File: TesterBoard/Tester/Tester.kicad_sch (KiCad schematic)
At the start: 18 parts, among them Q1 LM7805CT_NOPB, SW1 SW_DIP_x04, U1 74HC14N, U2 Z80CPU

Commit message: oscillator
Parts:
- added Y1: ATS08A-E, ATS08A-E:XTAL_HC49P488W43L1085T450H368, symbol ATS08A-E:ATS08A-E
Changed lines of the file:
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@@
+	)
+	(symbol
+		(lib_id "ATS08A-E:ATS08A-E")
+		(at 142.24 87.63 0)
+		(unit 1)
+		(exclude_from_sim no)
+		(in_bom yes)
+		(on_board yes)
+		(dnp no)
+		(fields_autoplaced yes)
+		(property "Reference" "Y1"
+			(at 142.24 80.01 0)
+			(effects
+				(font
+					(size 1.27 1.27)
+				)
+			)
+		)
+		(property "Value" "ATS08A-E"
+			(at 142.24 82.55 0)
+			(effects
+				(font
+					(size 1.27 1.27)
+				)
+			)
+		)
+		(property "Footprint" "ATS08A-E:XTAL_HC49P488W43L1085T450H368"
+			(at 142.24 87.63 0)
+			(effects
+				(font
+					(size 1.27 1.27)
+				)
+				(justify bottom)
+				(hide yes)
+			)
+		)
+		(property "Datasheet" ""
+			(at 142.24 87.63 0)
+			(effects
+				(font
+					(size 1.27 1.27)
+				)
+				(hide yes)
+			)
+		)
+		(property "Description" ""
+			(at 142.24 87.63 0)
+			(effects
+				(font
+					(size 1.27 1.27)
+				)
+				(hide yes)
+			)
+		)
+		(property "MAXIMUM_PACKAGE_HEIGHT" "3.68mm"
+			(at 142.24 87.63 0)
+			(effects
+				(font
+					(size 1.27 1.27)
+				)
+				(justify bottom)
+				(hide yes)
+			)
+		)
+		(property "STANDARD" "IPC-7351B"
+			(at 142.24 87.63 0)
+			(effects
+				(font
+					(size 1.27 1.27)
+				)
+				(justify bottom)
+				(hide yes)
+			)
+		)
+		(property "PARTREV" "M"
+			(at 142.24 87.63 0)
+			(effects
+				(font
+					(size 1.27 1.27)
+				)
+				(justify bottom)
+				(hide yes)
+			)
+		)
+		(property "MP" "ATS08A-E"
+			(at 142.24 87.63 0)
+			(effects
+				(font
+					(size 1.27 1.27)
+				)
+				(justify bottom)
+				(hide yes)
+			)
+		)
+		(property "MANUFACTURER" "CTS-Frequency Controls"
+			(at 142.24 87.63 0)
+			(effects
+				(font
+					(size 1.27 1.27)
+				)
+				(justify bottom)
+				(hide yes)
+			)
+		)
+		(property "DESCRIPTION" "8MHz ±30ppm Crystal 20pF 60 Ohms HC-49/US"
+			(at 142.24 87.63 0)
+			(effects
+				(font
+					(size 1.27 1.27)
+				)
+				(justify bottom)
+				(hide yes)
+			)
+		)
+		(pin "2"
+		)
+		(pin "1"
+		)
+		(instances
+			(project ""
+				(path "/806dc3e0-8575-4e5d-8446-51f379cb8ec6"
+					(reference "Y1")
+					(unit 1)
+				)
+			)
+		)
 	)
 	(symbol

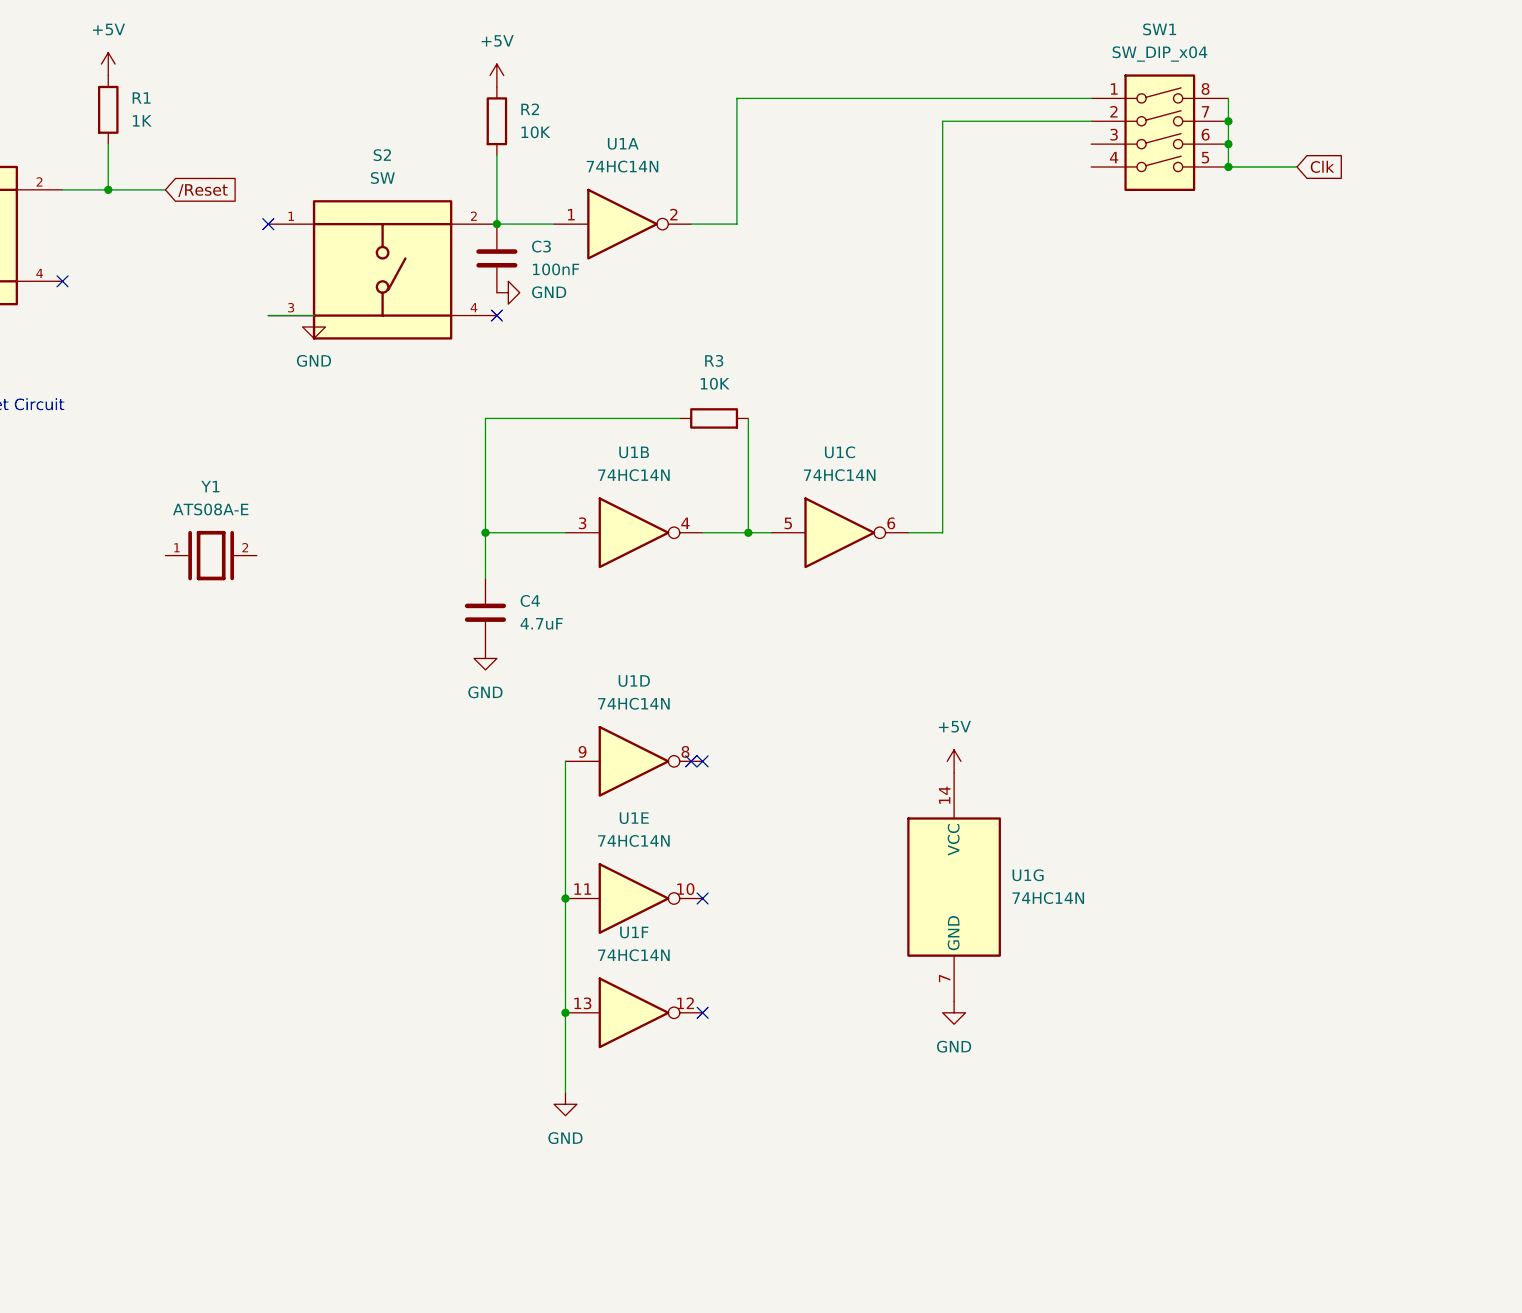
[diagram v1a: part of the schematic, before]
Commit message: redoing clock for tester
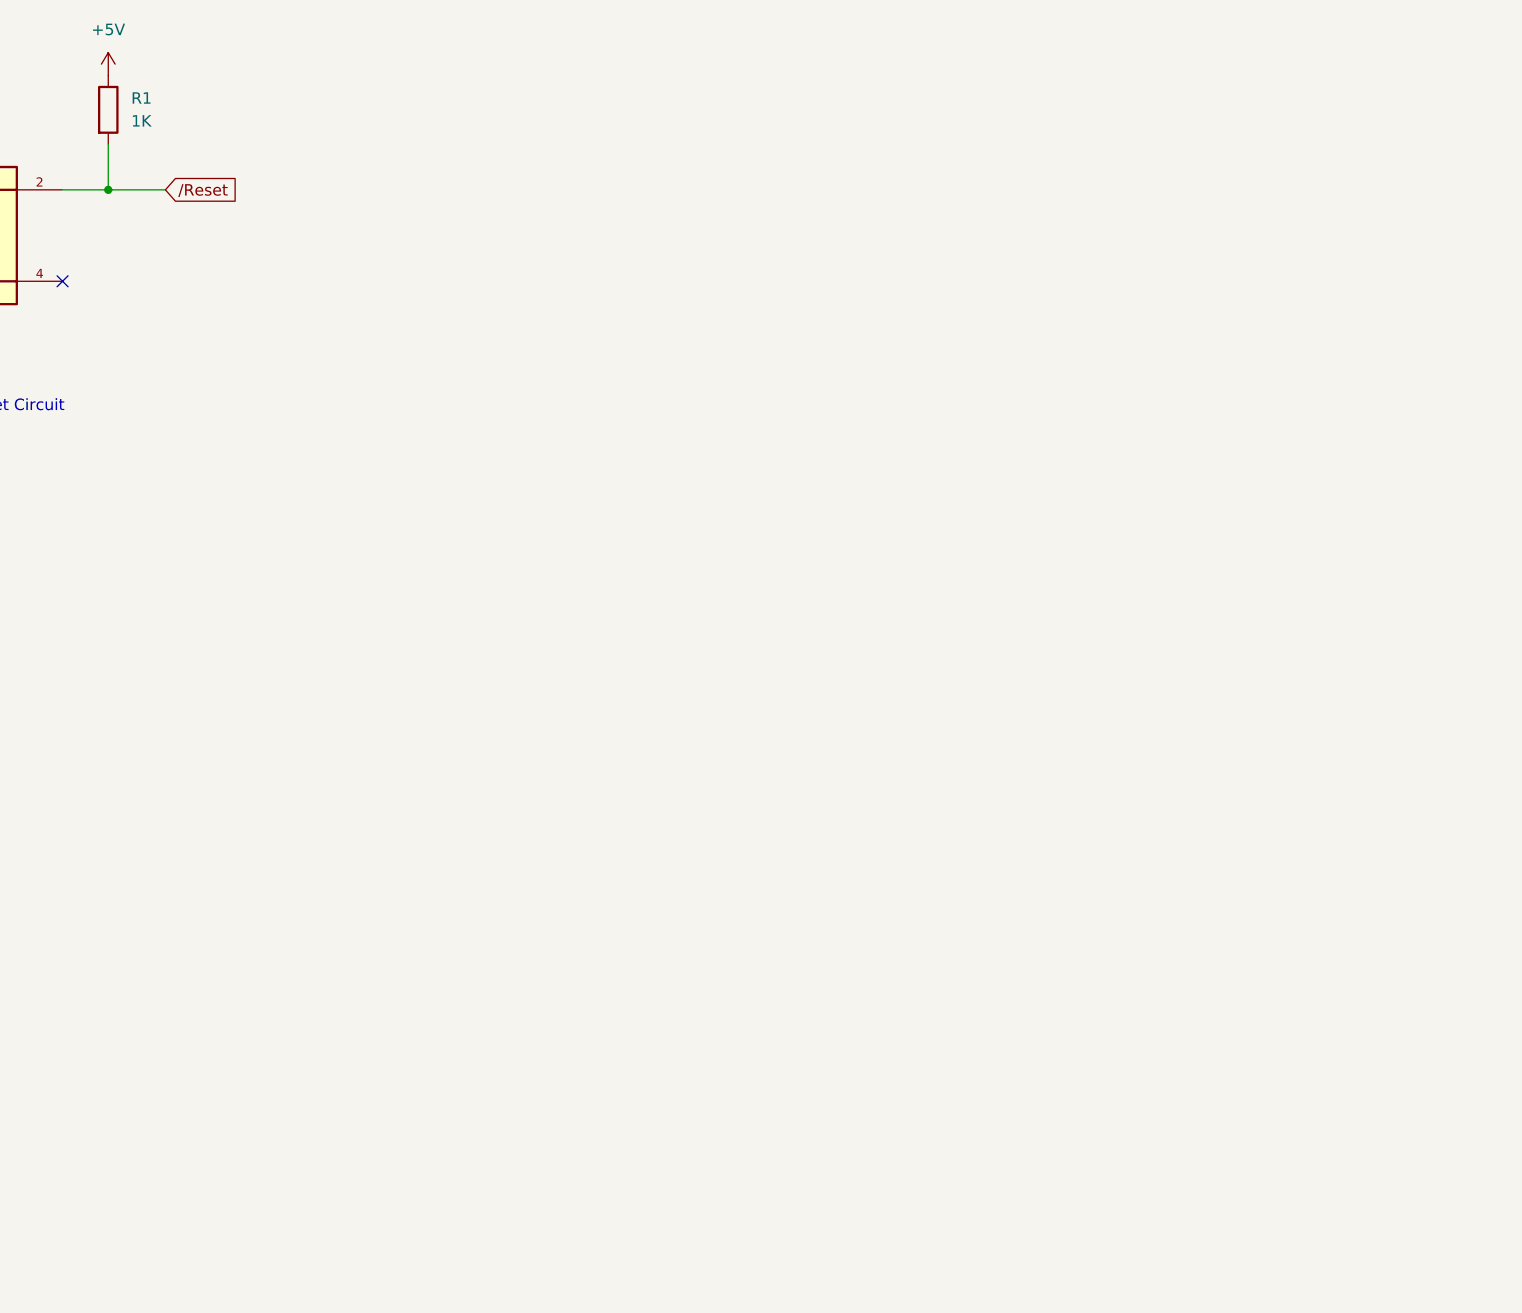
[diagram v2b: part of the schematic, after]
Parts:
- removed C3: 100nF, symbol Device:C
- removed C4: 4.7uF, symbol Device:C
- removed R2, R3: 10K, symbol Device:R
- removed S2: SW, TS02-66-60-BK-160-LCR-D:SW_TS02-66-60-BK-160-LCR-D, symbol Tactile_Button:TS02-66-60-BK-160-LCR-D
- removed SW1: SW_DIP_x04, symbol Switch:SW_DIP_x04
- removed U1: 74HC14N, symbol 74xx:74LS04
- removed Y1: ATS08A-E, ATS08A-E:XTAL_HC49P488W43L1085T450H368, symbol ATS08A-E:ATS08A-E
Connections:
- no-connect marks 10 -> 4

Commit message: pcb stuff
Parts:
- added J1: Conn_01x03, symbol Connector_Generic:Conn_01x03
- added Y1: ACH-4.000MHZ-EK, ACH-4.000MHZ-EK:XTAL_ACH-4.000MHZ-EK, symbol ACH-4.000MHZ-EK:ACH-4.000MHZ-EK
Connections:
- net +5V: now also Y1.1 (TRI-STATE/NC), Y1.8 (VDD)
- net Clk: now also J1.2 (Pin_2)
- net GND: now also Y1.4 (CASE_GND)
- net Address11: now reaches U2.1 (A11)
- net Data6: now reaches U2.10 (D6)
- net Data2: now reaches U2.12 (D2)
- net Data7: now reaches U2.13 (D7)
- net Data0: now reaches U2.14 (D0)
- net Data1: now reaches U2.15 (D1)
- net Address12: now reaches U2.2 (A12)
- net Address13: now reaches U2.3 (A13)
- net Address0: now reaches U2.30 (A0)
- net Address1: now reaches U2.31 (A1)
- net Address2: now reaches U2.32 (A2)
- net Address3: now reaches U2.33 (A3)
- net Address4: now reaches U2.34 (A4)
- net Address5: now reaches U2.35 (A5)
- net Address6: now reaches U2.36 (A6)
- net Address7: now reaches U2.37 (A7)
- net Address8: now reaches U2.38 (A8)
- net Address9: now reaches U2.39 (A9)
- net Address14: now reaches U2.4 (A14)
- net Address10: now reaches U2.40 (A10)
- net Address15: now reaches U2.5 (A15)
- net Data4: now reaches U2.7 (D4)
- net Data3: now reaches U2.8 (D3)
- net Data5: now reaches U2.9 (D5)
- new net EXTERNAL_CLOCK: J1.3 (Pin_3)
- new net OSC_CLOCK: J1.1 (Pin_1), Y1.5 (OUTPUT)

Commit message: schematic done
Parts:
- removed J1: Conn_01x03, symbol Connector_Generic:Conn_01x03
- removed Q1: LM7805CT_NOPB, LM7805CT:TO254P1054X470X2600-3, symbol LM7805CT_NOPB:LM7805CT_NOPB
- removed S1: SW, TS02-66-60-BK-160-LCR-D:SW_TS02-66-60-BK-160-LCR-D, symbol Tactile_Button:TS02-66-60-BK-160-LCR-D
- added C4: 100nF, Capacitor_THT:CP_Radial_D4.0mm_P2.00mm, symbol Device:C
- added D1, D10, D11, D12, D13, D14, D15, D16, D17, D18, D19, D2, D20, D21, D22, D23, D24, D25, D26, D27, D28, D29, D3, D30, D31, D32, D33, D34, D4, D5, D6, D7, D8, D9: LED, ECE445L:LED_D5.0mm, symbol Device:LED
- added J1, J3: Conn_01x03_Pin, Connector_PinHeader_2.54mm:PinHeader_1x03_P2.54mm_Vertical, symbol Connector:Conn_01x03_Pin
- added J2: PJ-102A, Z80_Tester_Footprints:CUI_PJ-102A, symbol Connector:PJ-102A
- added J4, J5, J6, J7: Conn_01x02_Pin, Connector_PinHeader_2.54mm:PinHeader_1x02_P2.54mm_Vertical, symbol Connector:Conn_01x02_Pin
- added J8: Conn_01x16_Pin, Connector_PinHeader_2.54mm:PinHeader_1x16_P2.54mm_Vertical, symbol Connector:Conn_01x16_Pin
- added J9: Conn_01x08_Pin, Connector_PinHeader_2.54mm:PinHeader_1x08_P2.54mm_Vertical, symbol Connector:Conn_01x08_Pin
- added R16, R17, R18, R19, R2, R20, R21, R22, R23, R24, R25, R26, R27, R28, R29, R30, R31, R32, R33, R34, R35, R36, R37, R38, R39, R40, R41, R42, R43, R44, R45, R46, R47, R48, R49, R50: 1K, ECE445L:R_Axial_DIN0204_L3.6mm_D1.6mm_P7.62mm_Horizontal, symbol Device:R
- added S2: B3F-4050, Button_Switch_THT:SW_PUSH_6mm, symbol Switch:SW_Push
- added SW1: SW_Push, Button_Switch_THT:SW_PUSH_6mm, symbol Switch:SW_Push
- added TP1, TP10, TP11, TP2, TP3, TP4, TP5, TP6, TP7, TP8, TP9: TestPoint, Connector_Pin:Pin_D1.0mm_L10.0mm, symbol Connector:TestPoint
- added U1: L7805, LM7805CT:TO254P1054X470X2600-3, symbol Regulator_Linear:L7805
- C1, C2, C5: footprint (none) -> Capacitor_THT:CP_Radial_D4.0mm_P2.00mm
- R1, R4, R5, R6, R7: footprint (none) -> ECE445L:R_Axial_DIN0204_L3.6mm_D1.6mm_P7.62mm_Horizontal
- U2: footprint (none) -> Socket:3M_Textool_240-1288-00-0602J_2x20_P2.54mm
- Y1: footprint ACH-4.000MHZ-EK:XTAL_ACH-4.000MHZ-EK -> Z80_Tester_Footprints:XTAL_ACH-4.000MHZ-EK
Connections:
- net +5V: now also C4.2, J3.2 (Pin_2), R39.1, R41.1, R42.1, R43.1, R44.1, R45.1, R46.1, R47.1, R48.1, R49.1, R50.1; no longer C2.1, C5.1
- net +9V: now also J2.1, U1.1 (IN)
- net Address0: now also J8.1 (Pin_1), R23.2
- net Address1: now also J8.2 (Pin_2), R24.2
- net Address10: now also J8.11 (Pin_11), R33.2
- net Address11: now also J8.12 (Pin_12), R34.2
- net Address12: now also J8.13 (Pin_13), R35.2
- net Address13: now also J8.14 (Pin_14), R36.2
- net Address14: now also J8.15 (Pin_15), R37.2
- net Address15: now also J8.16 (Pin_16), R38.2
- net Address2: now also J8.3 (Pin_3), R25.2
- net Address3: now also J8.4 (Pin_4), R26.2
- net Address4: now also J8.5 (Pin_5), R27.2
- net Address5: now also J8.6 (Pin_6), R28.2
- net Address6: now also J8.7 (Pin_7), R29.2
- net Address7: now also J8.8 (Pin_8), R30.2
- net Address8: now also J8.9 (Pin_9), R31.2
- net Address9: now also J8.10 (Pin_10), R32.2
- net Clk: now also J1.2 (Pin_2), R40.2, TP2.1
- net Data0: now also J9.1 (Pin_1), R2.2
- net Data1: now also J9.2 (Pin_2), R16.2
- net Data2: now also J9.3 (Pin_3), R17.2
- net Data3: now also J9.4 (Pin_4), R18.2
- net Data4: now also J9.5 (Pin_5), R19.2
- net Data5: now also J9.6 (Pin_6), R20.2
- net Data6: now also J9.7 (Pin_7), R21.2
- net Data7: now also J9.8 (Pin_8), R22.2
- net EXTERNAL_CLOCK: now also J1.1 (Pin_1), J6.1 (Pin_1), J6.2 (Pin_2)
- net GND: now also C4.1, D1.1 (K), D10.1 (K), D11.1 (K), D12.1 (K), D13.1 (K), D14.1 (K), D15.1 (K), D16.1 (K), D17.1 (K), D18.1 (K), D19.1 (K), D2.1 (K), D20.1 (K), D21.1 (K), D22.1 (K), D23.1 (K), D24.1 (K), D3.1 (K), D4.1 (K), D5.1 (K), D6.1 (K), D7.1 (K), D8.1 (K), D9.1 (K), J2.2, J5.1 (Pin_1), J5.2 (Pin_2), J7.1 (Pin_1), J7.2 (Pin_2), R40.1, S2.1, SW1.1, U1.2 (GND)
- net OSC_CLOCK: now also J1.3 (Pin_3)
- net /Halt: now also D28.1 (K), TP4.1
- net /IOREQ: now also D32.1 (K), TP8.1
- net /M1: now also D27.1 (K), TP3.1
- net /MREQ: now also D31.1 (K), TP7.1
- net /RD: now also D29.1 (K), TP5.1
- net /Reset: now also D25.1 (K), R50.2, S2.2, SW1.2, TP1.1
- net /WR: now also D30.1 (K), TP6.1
- net /INT: now reaches R5.1, U2.16 (~{INT})
- net /INT: now also D33.1 (K), TP10.1
- net /NMI: now reaches R4.2, U2.17 (~{NMI})
- net /NMI: now also D26.1 (K), TP9.1
- net /WAIT: now reaches R6.2, U2.24 (~{WAIT})
- net /WAIT: now also D34.1 (K), TP11.1
- new net: D18.2 (A), R32.1
- new net: D16.2 (A), R30.1
- new net: D22.2 (A), R36.1
- new net: D34.2 (A), R49.2
- new net: D3.2 (A), R17.1
- new net: D32.2 (A), R46.2
- new net: D33.2 (A), R48.2
- new net: D28.2 (A), R42.2
- new net: D5.2 (A), R19.1
- new net: D1.2 (A), R2.1
- new net: D30.2 (A), R44.2
- new net: D21.2 (A), R35.1
- new net: D17.2 (A), R31.1
- new net: D4.2 (A), R18.1
- new net: D15.2 (A), R29.1
- new net: D27.2 (A), R41.2
- new net: D26.2 (A), R47.2
- new net: D25.2 (A), R39.2
- new net: D8.2 (A), R22.1
- new net: D29.2 (A), R43.2
- new net: D7.2 (A), R21.1
- new net: D2.2 (A), R16.1
- new net: D6.2 (A), R20.1
- new net: D9.2 (A), R23.1
- new net: D13.2 (A), R27.1
- new net: D14.2 (A), R28.1
- new net: D12.2 (A), R26.1
- new net: D11.2 (A), R25.1
- new net: D10.2 (A), R24.1
- new net: D19.2 (A), R33.1
- new net: D24.2 (A), R38.1
- new net: D31.2 (A), R45.2
- new net: D23.2 (A), R37.1
- new net: D20.2 (A), R34.1
- new net Barrel_5V: C2.1, C5.1, J3.1 (Pin_1), U1.3 (OUT)
- new net Ext_5V: J3.3 (Pin_3), J4.1 (Pin_1), J4.2 (Pin_2)
- no-connect marks 4 -> 3
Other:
- note added: "Clock Select Jumper"
- note added: "Debug LEDs"
- note added: "Debug Pins"
- note added: "External Clock Pins"
- note added: "External Power Pins"
- note added: "On Board Oscillator"
- note added: "Power Jumper"
- moved on the sheet: R1, Y1
